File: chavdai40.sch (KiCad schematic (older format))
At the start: 7 parts

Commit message: make a schematic
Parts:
- removed C?: 100n, symbol Device:C_Small
- removed U?: USBLC6-2SC6, Package_TO_SOT_SMD:SOT-23-6, symbol Power_Protection:USBLC6-2SC6
- added C1, C7, C9: 100n, symbol Device:C_Small
- added C2, C8: 4.7u, symbol Device:C_Small
- added C3: 1u, symbol Device:C_Small
- added C4: 10n, symbol Device:C_Small
- added F1: MF-NSMF050-2, symbol Device:Polyfuse_Small
- added R1, R2: 22, symbol Device:R_Small
- added R3, R5: 5.1k, symbol Device:R_Small
- added R4: 10k, symbol Device:R_Small
- added SW_BOOT1, SW_RESET1: TS-1187A-B-A-B, symbol Switch:SW_Push
- added U2: PRTR5V0U4D, Package_TO_SOT_SMD:SOT-23-6, symbol miyajima:PRTR5V0U4D
- added USB1: HRO-TYPE-C-31-M-12, symbol Type-C:HRO-TYPE-C-31-M-12
- C5: renamed from C?; value 100n -> 1u
- C6: renamed from C?; value 100n -> 22u
- gave numbers to parts that had none: 3
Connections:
- net labels removed: BOOT0, DBus+, DBus-
- wire segments 14 -> 78
- no-connect marks 2 -> 4
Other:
- moved on the sheet: C5, C6, J1, U1, U3

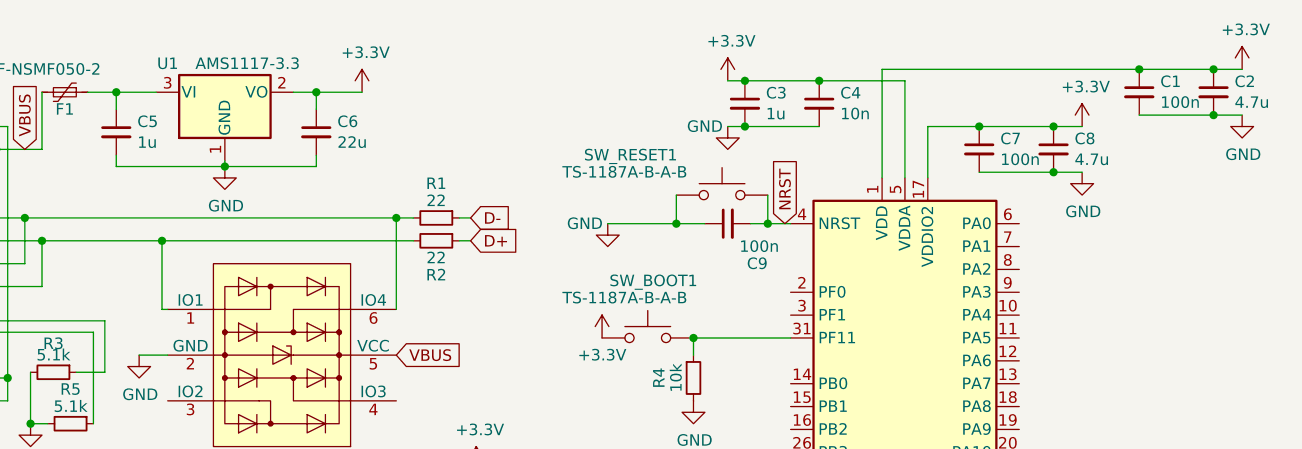
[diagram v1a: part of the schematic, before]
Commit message: usb 22ohm register remove; pas-con remove
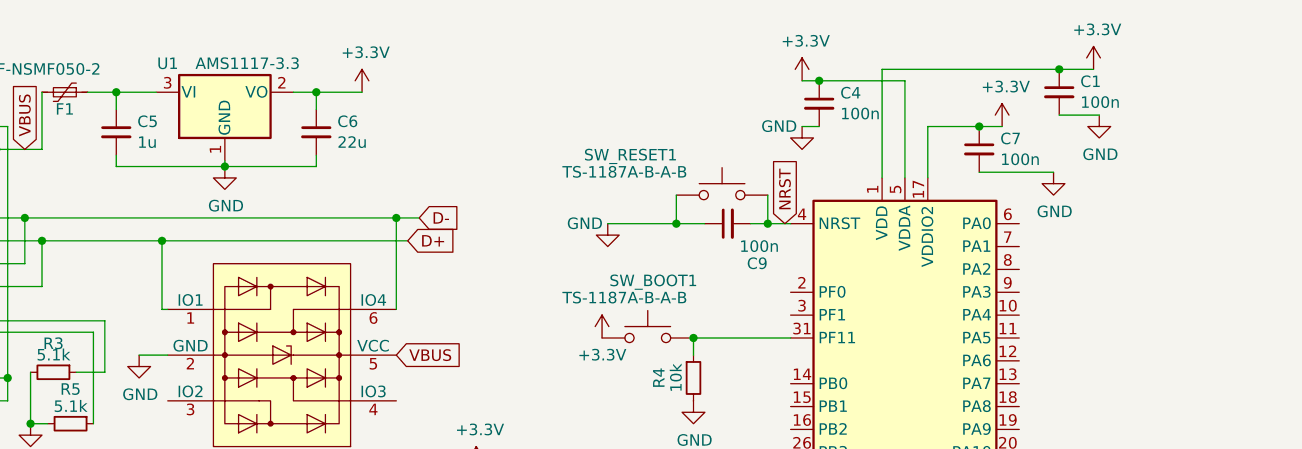
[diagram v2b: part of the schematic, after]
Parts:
- removed C2, C8: 4.7u, symbol Device:C_Small
- removed C3: 1u, symbol Device:C_Small
- removed R1, R2: 22, symbol Device:R_Small
- C4: value 10n -> 100n
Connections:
- net D+: now also U2.1 (IO1), USB1.6 (DP1), USB1.8 (DP2)
- net D-: now also U2.6 (IO4), USB1.5 (DN2), USB1.7 (DN1)
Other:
- moved on the sheet: C1
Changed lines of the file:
@@
 	1    0    0    -1
 $EndComp
-Text GLabel 3350 1425 2    50   Input ~ 0
+Text GLabel 3125 1425 2    50   Input ~ 0
 D-
-Text GLabel 3350 1525 2    50   Input ~ 0
+Text GLabel 3075 1525 2    50   Input ~ 0
 D+
 Text GLabel 3025 2025 2    50   Input ~ 0
@@
 L power:+3.3V #PWR0106
 U 1 1 5EADDDB4
-P 6725 775
-F 0 "#PWR0106" H 6725 625 50  0001 C CNN
-F 1 "+3.3V" H 6740 948 50  0000 C CNN
-F 2 "" H 6725 775 50  0001 C CNN
-F 3 "" H 6725 775 50  0001 C CNN
-	1    6725 775
+P 6075 775
+F 0 "#PWR0106" H 6075 625 50  0001 C CNN
+F 1 "+3.3V" H 6090 948 50  0000 C CNN
+F 2 "" H 6075 775 50  0001 C CNN
+F 3 "" H 6075 775 50  0001 C CNN
+	1    6075 775
 	1    0    0    -1
 $EndComp
@@
 L Device:C_Small C1
 U 1 1 5EB230F9
-P 6275 875
-F 0 "C1" H 6367 921 50  0000 L CNN
-F 1 "100n" H 6367 830 50  0000 L CNN
-F 2 "" H 6275 875 50  0001 C CNN
-F 3 "~" H 6275 875 50  0001 C CNN
-	1    6275 875
+P 5925 875
+F 0 "C1" H 6017 921 50  0000 L CNN
+F 1 "100n" H 6017 830 50  0000 L CNN
+F 2 "" H 5925 875 50  0001 C CNN
+F 3 "~" H 5925 875 50  0001 C CNN
+	1    5925 875
 	1    0    0    -1
 $EndComp
@@
 P 4875 925
 F 0 "C4" H 4967 971 50  0000 L CNN
-F 1 "10n" H 4967 880 50  0000 L CNN
+F 1 "100n" H 4967 880 50  0000 L CNN
 F 2 "" H 4875 925 50  0001 C CNN
 F 3 "~" H 4875 925 50  0001 C CNN
@@
 	1    0    0    -1
 $EndComp
-$Comp
-L Device:C_Small C2
-U 1 1 5EB343B0
-P 6600 875
-F 0 "C2" H 6692 921 50  0000 L CNN
-F 1 "4.7u" H 6692 830 50  0000 L CNN
-F 2 "" H 6600 875 50  0001 C CNN
-F 3 "~" H 6600 875 50  0001 C CNN
-	1    6600 875
-	1    0    0    -1
-$EndComp
 Wire Wire Line
 	5150 1250 5150 775
-Wire Wire Line
-	6725 975  6600 975
-Connection ~ 6275 775
+Connection ~ 5925 775
 $Comp
 L power:GND #PWR0110
 U 1 1 5EB22A4F
-P 6725 975
-F 0 "#PWR0110" H 6725 725 50  0001 C CNN
-F 1 "GND" H 6730 802 50  0000 C CNN
-F 2 "" H 6725 975 50  0001 C CNN
-F 3 "" H 6725 975 50  0001 C CNN
-	1    6725 975
-	1    0    0    -1
-$EndComp
-Connection ~ 6600 775
-Wire Wire Line
-	6600 775  6725 775
-Connection ~ 6600 975
-Wire Wire Line
-	5150 775  6275 775
-$Comp
-L power:+3.3V #PWR0111
-U 1 1 5EB947AF
-P 4475 825
-F 0 "#PWR0111" H 4475 675 50  0001 C CNN
-F 1 "+3.3V" H 4490 998 50  0000 C CNN
-F 2 "" H 4475 825 50  0001 C CNN
-F 3 "" H 4475 825 50  0001 C CNN
-	1    4475 825
-	1    0    0    -1
-$EndComp
-$Comp
-L power:GND #PWR0112
-U 1 1 5EB952C2
-P 4475 1025
-F 0 "#PWR0112" H 4475 775 50  0001 C CNN
-F 1 "GND" H 4375 1025 50  0000 C CNN
-F 2 "" H 4475 1025 50  0001 C CNN
-F 3 "" H 4475 1025 50  0001 C CNN
-	1    4475 1025
-	1    0    0    -1
-$EndComp
-Wire Wire Line
-	6600 975  6275 975
-Wire Wire Line
-	6275 775  6600 775
+P 6100 975
+F 0 "#PWR0110" H 6100 725 50  0001 C CNN
+F 1 "GND" H 6105 802 50  0000 C CNN
+F 2 "" H 6100 975 50  0001 C CNN
+F 3 "" H 6100 975 50  0001 C CNN
+	1    6100 975
+	1    0    0    -1
+$EndComp
+Wire Wire Line
+	5150 775  5925 775
 Wire Wire Line
 	5250 1250 5250 825
@@
 	5250 825  4875 825
 Connection ~ 4875 825
-Wire Wire Line
-	4875 825  4550 825
-Wire Wire Line
-	4475 1025 4550 1025
-$Comp
-L Device:C_Small C3
-U 1 1 5EBA045E
-P 4550 925
-F 0 "C3" H 4642 971 50  0000 L CNN
-F 1 "1u" H 4642 880 50  0000 L CNN
-F 2 "" H 4550 925 50  0001 C CNN
-F 3 "~" H 4550 925 50  0001 C CNN
-	1    4550 925
-	1    0    0    -1
-$EndComp
-Connection ~ 4550 825
-Wire Wire Line
-	4550 825  4475 825
-Connection ~ 4550 1025
-Wire Wire Line
-	4550 1025 4875 1025
 $Comp
 L power:+3.3V #PWR0113
 U 1 1 5EBA0E93
-P 6025 1025
-F 0 "#PWR0113" H 6025 875 50  0001 C CNN
-F 1 "+3.3V" H 6040 1198 50  0000 C CNN
-F 2 "" H 6025 1025 50  0001 C CNN
-F 3 "" H 6025 1025 50  0001 C CNN
-	1    6025 1025
+P 5675 1025
+F 0 "#PWR0113" H 5675 875 50  0001 C CNN
+F 1 "+3.3V" H 5690 1198 50  0000 C CNN
+F 2 "" H 5675 1025 50  0001 C CNN
+F 3 "" H 5675 1025 50  0001 C CNN
+	1    5675 1025
 	1    0    0    -1
 $EndComp
@@
 $EndComp
 $Comp
-L Device:C_Small C8
-U 1 1 5EBA0EA7
-P 5900 1125
-F 0 "C8" H 5992 1171 50  0000 L CNN
-F 1 "4.7u" H 5992 1080 50  0000 L CNN
-F 2 "" H 5900 1125 50  0001 C CNN
-F 3 "~" H 5900 1125 50  0001 C CNN
-	1    5900 1125
-	1    0    0    -1
-$EndComp
-Wire Wire Line
-	6025 1225 5900 1225
-$Comp
 L power:GND #PWR0114
 U 1 1 5EBA0EB3
-P 6025 1225
-F 0 "#PWR0114" H 6025 975 50  0001 C CNN
-F 1 "GND" H 6030 1052 50  0000 C CNN
-F 2 "" H 6025 1225 50  0001 C CNN
-F 3 "" H 6025 1225 50  0001 C CNN
-	1    6025 1225
-	1    0    0    -1
-$EndComp
-Connection ~ 5900 1025
-Wire Wire Line
-	5900 1025 6025 1025
-Connection ~ 5900 1225
-Wire Wire Line
-	5900 1225 5575 1225
-Wire Wire Line
-	5575 1025 5900 1025
+P 5900 1225
+F 0 "#PWR0114" H 5900 975 50  0001 C CNN
+F 1 "GND" H 5905 1052 50  0000 C CNN
+F 2 "" H 5900 1225 50  0001 C CNN
+F 3 "" H 5900 1225 50  0001 C CNN
+	1    5900 1225
+	1    0    0    -1
+$EndComp
 Wire Wire Line
 	5350 1250 5350 1025
@@
 	5350 1025 5575 1025
 Connection ~ 5575 1025
-$Comp
-L Device:R_Small R2
-U 1 1 5EBBF762
-P 3200 1525
-F 0 "R2" V 3350 1525 50  0000 C CNN
-F 1 "22" V 3275 1525 50  0000 C CNN
-F 2 "" H 3200 1525 50  0001 C CNN
-F 3 "~" H 3200 1525 50  0001 C CNN
-	1    3200 1525
-	0    1    1    0
-$EndComp
-$Comp
-L Device:R_Small R1
-U 1 1 5EBBFCAE
-P 3200 1425
-F 0 "R1" V 3050 1425 50  0000 C CNN
-F 1 "22" V 3125 1425 50  0000 C CNN
-F 2 "" H 3200 1425 50  0001 C CNN
-F 3 "~" H 3200 1425 50  0001 C CNN
-	1    3200 1425
-	0    1    1    0
-$EndComp
-Wire Wire Line
-	3300 1425 3350 1425
-Wire Wire Line
-	3300 1525 3350 1525
 $Comp
 L miyajima:PRTR5V0U4D U2
@@
 Connection ~ 3025 1425
 Wire Wire Line
-	3025 1425 3100 1425
-Wire Wire Line
 	2000 1525 2000 1825
 Connection ~ 2000 1525
-Wire Wire Line
-	2000 1525 3100 1525
 Wire Wire Line
 	1200 2325 1200 2225
@@
 Wire Wire Line
 	5750 2750 6200 2750
+Wire Wire Line
+	3025 1425 3125 1425
+Wire Wire Line
+	2000 1525 3075 1525
+Wire Wire Line
+	5925 775  6075 775
+Wire Wire Line
+	5925 975  6100 975
+Wire Wire Line
+	5575 1025 5675 1025
+Wire Wire Line
+	5575 1225 5900 1225
+Wire Wire Line
+	4800 1025 4875 1025
+$Comp
+L power:GND #PWR0112
+U 1 1 5EB952C2
+P 4800 1025
+F 0 "#PWR0112" H 4800 775 50  0001 C CNN
+F 1 "GND" H 4700 1025 50  0000 C CNN
+F 2 "" H 4800 1025 50  0001 C CNN
+F 3 "" H 4800 1025 50  0001 C CNN
+	1    4800 1025
+	1    0    0    -1
+$EndComp
+$Comp
+L power:+3.3V #PWR0111
+U 1 1 5EB947AF
+P 4800 825
+F 0 "#PWR0111" H 4800 675 50  0001 C CNN
+F 1 "+3.3V" H 4815 998 50  0000 C CNN
+F 2 "" H 4800 825 50  0001 C CNN
+F 3 "" H 4800 825 50  0001 C CNN
+	1    4800 825
+	1    0    0    -1
+$EndComp
+Wire Wire Line
+	4800 825  4875 825
 $EndSCHEMATC

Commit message: 2020-05-09 PCB dekita
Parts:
- removed U2: PRTR5V0U4D, Package_TO_SOT_SMD:SOT-23-6, symbol miyajima:PRTR5V0U4D
- added D1, D10, D11, D12, D13, D14, D15, D16, D17, D18, D19, D2, D20, D21, D22, D23, D24, D25, D26, D27, D28, D29, D3, D30, D31, D32, D33, D34, D35, D36, D37, D38, D39, D4, D40, D41, D42, D43, D44, D5, D6, D7, D8, D9: SOD-123, Diode_SMD:D_SOD-323F, symbol Device:D_Small
- added ESD1, ESD2: ESDAXLC6-1BT2, Diode_SMD:D_0402_1005Metric, symbol Diode:1.5KExxCA
- added MX1, MX13: MX-NoLED, MX_Only:MXOnly-1.5U-NoLED, symbol MX_Alps_Hybrid:MX-NoLED
- added MX10, MX11, MX12, MX15, MX16, MX17, MX18, MX19, MX2, MX20, MX21, MX22, MX23, MX24, MX27, MX28, MX29, MX3, MX30, MX31, MX32, MX33, MX34, MX35, MX4, MX5, MX6, MX7, MX8, MX9: MX-NoLED, MX_Only:MXOnly-1U-NoLED, symbol MX_Alps_Hybrid:MX-NoLED
- added MX14: MX-NoLED, MX_Only:MXOnly-1.75U-NoLED, symbol MX_Alps_Hybrid:MX-NoLED
- added MX25, MX26, MX40: MX-NoLED, MX_Only:MXOnly-2.25U-NoLED, symbol MX_Alps_Hybrid:MX-NoLED
- added MX36, MX37, MX38, MX39, MX42, MX43, MX44: MX-NoLED, MX_Only:MXOnly-1.25U-NoLED, symbol MX_Alps_Hybrid:MX-NoLED
- added MX41: MX-NoLED, MX_Only:MXOnly-2.75U-NoLED, symbol MX_Alps_Hybrid:MX-NoLED
- added MX45: MX-NoLED, MX_Only:MXOnly-6.25U-NoLED, symbol MX_Alps_Hybrid:MX-NoLED
- C1: footprint (none) -> Capacitor_SMD:C_0603_1608Metric
- C2: renamed from C4; footprint (none) -> Capacitor_SMD:C_0603_1608Metric
- C3: renamed from C5; value 1u -> 1u mlcc; footprint (none) -> Capacitor_SMD:C_0805_2012Metric
- C4: renamed from C6; value 22u -> 1u mlcc; footprint (none) -> Capacitor_SMD:C_0805_2012Metric
- C5: renamed from C7; footprint (none) -> Capacitor_SMD:C_0603_1608Metric
- C6: renamed from C9; footprint (none) -> Capacitor_SMD:C_0603_1608Metric
- F1: value MF-NSMF050-2 -> nSMD025; footprint (none) -> Fuse:Fuse_1206_3216Metric
- J1: footprint (none) -> Connector_PinHeader_1.27mm:PinHeader_2x05_P1.27mm_Vertical
- R1: renamed from R3; footprint (none) -> Resistor_SMD:R_0603_1608Metric
- R2: renamed from R4; footprint (none) -> Resistor_SMD:R_0603_1608Metric
- R3: renamed from R5; footprint (none) -> Resistor_SMD:R_0603_1608Metric
- SW_BOOT1, SW_RESET1: footprint (none) -> random-keyboard-parts:SKQGADE010
- U1: value AMS1117-3.3 -> XC6206P332MR; footprint Package_TO_SOT_SMD:SOT-223-3_TabPin2 -> Package_TO_SOT_SMD:TSOT-23
- USB1: footprint (none) -> Type-C:HRO-TYPE-C-31-M-12-HandSoldering
- renumbered U3 to U2
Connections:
- net D+: now also ESD2.2 (A2)
- net D-: now also ESD1.1 (A1)
- net GND: now also ESD1.2 (A2), ESD2.1 (A1)
- net COL9: now reaches U2.10 (PA4)
- net COL9: now also MX10.1 (COL), MX23.1 (COL), MX35.1 (COL), MX43.1 (COL)
- net COL8: now reaches U2.11 (PA5)
- net COL8: now also MX22.1 (COL), MX34.1 (COL), MX42.1 (COL), MX9.1 (COL)
- net COL7: now reaches U2.12 (PA6)
- net COL7: now also MX21.1 (COL), MX33.1 (COL), MX8.1 (COL)
- net COL6: now reaches U2.13 (PA7)
- net COL6: now also MX20.1 (COL), MX32.1 (COL), MX7.1 (COL)
- net COL5: now reaches U2.14 (PB0)
- net COL5: now also MX19.1 (COL), MX31.1 (COL), MX41.1 (COL), MX45.1 (COL), MX6.1 (COL)
- net COL4: now reaches U2.15 (PB1)
- net COL4: now also MX18.1 (COL), MX30.1 (COL), MX5.1 (COL)
- net COL3: now reaches U2.16 (PB2)
- net COL3: now also MX17.1 (COL), MX29.1 (COL), MX4.1 (COL), MX40.1 (COL)
- net ROW1: now reaches U2.25 (PA15)
- net ROW1: now also D14.1 (K), D15.1 (K), D16.1 (K), D17.1 (K), D18.1 (K), D19.1 (K), D20.1 (K), D21.1 (K), D22.1 (K), D23.1 (K), D24.1 (K), D25.1 (K)
- net COL2: now reaches U2.26 (PB3)
- net COL2: now also MX16.1 (COL), MX28.1 (COL), MX3.1 (COL)
- net COL1: now reaches U2.27 (PB4)
- net COL1: now also MX15.1 (COL), MX2.1 (COL), MX27.1 (COL), MX39.1 (COL)
- net ROW2: now reaches U2.28 (PB5)
- net ROW2: now also D26.1 (K), D27.1 (K), D28.1 (K), D29.1 (K), D30.1 (K), D31.1 (K), D32.1 (K), D33.1 (K), D34.1 (K), D35.1 (K), D36.1 (K), D37.1 (K)
- net ROW3: now reaches U2.29 (PB6)
- net ROW3: now also D38.1 (K), D39.1 (K), D40.1 (K), D41.1 (K), D42.1 (K), D43.1 (K), D44.1 (K)
- net COL0: now reaches U2.32 (PB8)
- net COL0: now also MX1.1 (COL), MX14.1 (COL), MX26.1 (COL), MX38.1 (COL)
- net ROW0: now reaches U2.6 (PA0)
- net ROW0: now also D1.1 (K), D10.1 (K), D11.1 (K), D12.1 (K), D13.1 (K), D2.1 (K), D3.1 (K), D4.1 (K), D5.1 (K), D6.1 (K), D7.1 (K), D8.1 (K), D9.1 (K)
- net COL12: now reaches U2.7 (PA1)
- net COL12: now also MX13.1 (COL)
- net COL11: now reaches U2.8 (PA2)
- net COL11: now also MX12.1 (COL), MX25.1 (COL), MX37.1 (COL)
- net COL10: now reaches U2.9 (PA3)
- net COL10: now also MX11.1 (COL), MX24.1 (COL), MX36.1 (COL), MX44.1 (COL)
- new net: D41.2 (A), MX41.2 (ROW), MX45.2 (ROW)
- new net: D5.2 (A), MX5.2 (ROW)
- new net: D6.2 (A), MX6.2 (ROW)
- new net: D18.2 (A), MX18.2 (ROW)
- new net: D19.2 (A), MX19.2 (ROW)
- new net: D30.2 (A), MX30.2 (ROW)
- new net: D31.2 (A), MX31.2 (ROW)
- new net: D42.2 (A), MX42.2 (ROW)
- new net: D7.2 (A), MX7.2 (ROW)
- new net: D20.2 (A), MX20.2 (ROW)
- new net: D8.2 (A), MX8.2 (ROW)
- new net: D9.2 (A), MX9.2 (ROW)
- new net: D10.2 (A), MX10.2 (ROW)
- new net: D11.2 (A), MX11.2 (ROW)
- new net: D21.2 (A), MX21.2 (ROW)
- new net: D22.2 (A), MX22.2 (ROW)
- new net: D23.2 (A), MX23.2 (ROW)
- new net: D24.2 (A), MX24.2 (ROW)
- new net: D43.2 (A), MX43.2 (ROW)
- new net: D44.2 (A), MX44.2 (ROW)
- new net: D37.2 (A), MX37.2 (ROW)
- new net: D12.2 (A), MX12.2 (ROW)
- new net: D25.2 (A), MX25.2 (ROW)
- new net: D2.2 (A), MX2.2 (ROW)
- new net: D1.2 (A), MX1.2 (ROW)
- new net: D15.2 (A), MX15.2 (ROW)
- new net: D14.2 (A), MX14.2 (ROW)
- new net: D3.2 (A), MX3.2 (ROW)
- new net: D4.2 (A), MX4.2 (ROW)
- new net: D16.2 (A), MX16.2 (ROW)
- new net: D17.2 (A), MX17.2 (ROW)
- new net: D27.2 (A), MX27.2 (ROW)
- new net: D28.2 (A), MX28.2 (ROW)
- new net: D29.2 (A), MX29.2 (ROW)
- new net: D38.2 (A), MX38.2 (ROW)
- new net: D39.2 (A), MX39.2 (ROW)
- new net: D40.2 (A), MX40.2 (ROW)
- new net: D26.2 (A), MX26.2 (ROW)
- new net: D13.2 (A), MX13.2 (ROW)
- new net: D34.2 (A), MX34.2 (ROW)
- new net: D36.2 (A), MX36.2 (ROW)
- new net: D35.2 (A), MX35.2 (ROW)
- new net: D33.2 (A), MX33.2 (ROW)
- new net: D32.2 (A), MX32.2 (ROW)
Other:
- note added: ","
- note added: "-"
- note added: "."
- note added: "/"
- note added: "625 Space"
- note added: "Alt"
- note added: "B"
- note added: "BS"
- note added: "C"
- note added: "Ctrl"
- note added: "Delete"
- note added: "Enter"
- note added: "Esc"
- note added: "G"
- note added: "H"
- note added: "K"
- note added: "L1"
- note added: "M"
- note added: "N"
- note added: "Shift"
- note added: "Space"
- note added: "T"
- note added: "Tab"
- note added: "V"
- note added: "Win"
- note added: "X"
- note added: "Y"
- note added: "Z"
- moved on the sheet: J1

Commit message: tabun dekita
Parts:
- added SMT1, SMT2, SMT3: Tooling Hole, random-keyboard-parts:jlcpcb-tooling-hole, symbol Mechanical:MountingHole
- added logo1: Chavdai40%, Type-C:logo2-small, symbol Mechanical:MountingHole
- C1, C2: value 100n -> 100nF; footprint Capacitor_SMD:C_0603_1608Metric -> Capacitor_SMD:C_0402_1005Metric
- C3: renamed from C5; value 100n -> 100nF; footprint Capacitor_SMD:C_0603_1608Metric -> Capacitor_SMD:C_0402_1005Metric
- C4: renamed from C6; value 100n -> 100nF; footprint Capacitor_SMD:C_0603_1608Metric -> Capacitor_SMD:C_0402_1005Metric
- C5: renamed from C3; value 1u mlcc -> 1uF; footprint Capacitor_SMD:C_0805_2012Metric -> Capacitor_SMD:C_0603_1608Metric
- C6: renamed from C4; value 1u mlcc -> 1uF; footprint Capacitor_SMD:C_0805_2012Metric -> Capacitor_SMD:C_0603_1608Metric
- MX26, MX40: footprint MX_Only:MXOnly-2.25U-NoLED -> MX_Only:MXOnly-2.25U-ReversedStabilizers-NoLED
- MX41: footprint MX_Only:MXOnly-2.75U-NoLED -> MX_Only:MXOnly-2.75U-ReversedStabilizers-NoLED
- MX42: renamed from MX45; footprint MX_Only:MXOnly-6.25U-NoLED -> MX_Only:MXOnly-6.25U-ReversedStabilizers-NoLED
- renumbered MX42 to MX43, MX43 to MX44, MX44 to MX45, R2 to R1, R1 to R2, U2 to U1, U1 to U2
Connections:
- net VBUS: no longer names the net of F1.2, USB1.11 (VBUS), USB1.2 (VBUS)
- no-connect marks 4 -> 13
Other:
- moved on the sheet: C5, C6, ESD1, ESD2, F1, J1, R2, R3, U2, USB1

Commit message: create info.json
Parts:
- D1, D10, D11, D12, D13, D14, D15, D16, D17, D18, D19, D2, D20, D21, D22, D23, D24, D25, D26, D27, D28, D29, D3, D30, D31, D32, D33, D34, D35, D36, D37, D38, D39, D4, D40, D41, D42, D43, D44, D5, D6, D7, D8, D9: footprint Diode_SMD:D_SOD-323F -> Diode_SMD:D_SOD-123

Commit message: update chavdai pcb design(rev2)
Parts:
- removed J1: Conn_ARM_JTAG_SWD_10, Connector_PinHeader_1.27mm:PinHeader_2x05_P1.27mm_Vertical, symbol Connector:Conn_ARM_JTAG_SWD_10
- removed SMT1, SMT2, SMT3: Tooling Hole, random-keyboard-parts:jlcpcb-tooling-hole, symbol Mechanical:MountingHole
- removed U1: STM32F042K6U6, Package_DFN_QFN:QFN-32-1EP_5x5mm_P0.5mm_EP3.45x3.45mm, symbol MCU_ST_STM32F0:STM32F042K6Ux
- added J1: Conn_01x02, Connector_PinHeader_2.54mm:PinHeader_1x02_P2.54mm_Vertical, symbol Connector_Generic:Conn_01x02
- added J2: Conn_01x03, Connector_PinHeader_2.54mm:PinHeader_1x03_P2.54mm_Vertical, symbol Connector_Generic:Conn_01x03
- added U1: STM32F042K6T6, Package_QFP:LQFP-32_7x7mm_P0.8mm, symbol MCU_ST_STM32F0:STM32F042K6Tx
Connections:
- net +3V3: now also J1.2 (Pin_2), U1.1 (VDD), U1.17 (VDDIO2), U1.5 (VDDA)
- net COL0: now also U1.30 (PB7)
- net COL1: now also U1.27 (PB4)
- net COL10: now also U1.9 (PA3)
- net COL11: now also U1.8 (PA2)
- net COL12: now also U1.7 (PA1)
- net COL2: now also U1.26 (PB3)
- net COL3: now also U1.18 (PA8)
- net COL4: now also U1.15 (PB1)
- net COL5: now also U1.14 (PB0)
- net COL6: now also U1.13 (PA7)
- net COL7: now also U1.12 (PA6)
- net COL8: now also U1.11 (PA5)
- net COL9: now also U1.10 (PA4)
- net D+: now also U1.22 (PA12)
- net D-: now also U1.21 (PA11)
- net GND: now also J1.1 (Pin_1), U1.16 (VSS), U1.32 (VSSA)
- net NRST: now also J2.1 (Pin_1), U1.4 (NRST)
- net ROW0: now also U1.6 (PA0)
- net ROW1: now also U1.25 (PA15)
- net ROW2: now also U1.28 (PB5)
- net ROW3: now also U1.29 (PB6)
- net SWCLK: now also J2.2 (Pin_2), U1.24 (PA14)
- net SWDIO: now also J2.3 (Pin_3), U1.23 (PA13)
- net at R1.1, SW_BOOT1.2: now also U1.31 (PB8)
- no-connect marks 13 -> 9
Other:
- moved on the sheet: C1, C2, C3, C4, R1, SW_BOOT1, SW_RESET1, logo1
